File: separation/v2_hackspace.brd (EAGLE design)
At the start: 40.6 x 25.4 mm, 14 parts

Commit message: easy traces
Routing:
- net VSENSE: track 0.00 -> 36.5 mm
- net SERVO: track 0.00 -> 15.4 mm
- net VBAT: track 0.00 -> 13.2 mm
- net BUZZ: track 0.00 -> 9.01 mm
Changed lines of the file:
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@@
 <contactref element="SERCON" pad="2"/>
 <contactref element="C2" pad="2"/>
+<wire x1="-14.986" y1="3.556" x2="-14.986" y2="8.509" width="2.032" layer="16"/>
+<wire x1="-14.986" y1="8.509" x2="-15.113" y2="8.636" width="2.032" layer="16"/>
+<wire x1="-14.986" y1="3.556" x2="-14.986" y2="2.286" width="1.016" layer="16"/>
+<wire x1="-13.716" y1="1.016" x2="-11.684" y2="1.016" width="1.016" layer="16"/>
+<wire x1="-11.684" y1="1.016" x2="-9.661025" y2="3.038975" width="1.016" layer="16"/>
+<wire x1="-9.661025" y1="3.038975" x2="-9.661025" y2="3.184025" width="1.016" layer="16"/>
+<wire x1="-14.986" y1="2.286" x2="-13.716" y2="1.016" width="1.016" layer="16"/>
 <wire x1="-9.661025" y1="3.184025" x2="14.224" y2="14.605" width="0" layer="19" extent="1-1"/>
-<wire x1="-14.986" y1="3.556" x2="-9.661025" y2="3.184025" width="0" layer="19" extent="1-1"/>
-<wire x1="-15.113" y1="8.636" x2="-14.986" y2="3.556" width="0" layer="19" extent="1-1"/>
 <wire x1="-14.859" y1="19.431" x2="-15.113" y2="8.636" width="0" layer="19" extent="1-1"/>
 </signal>
@@
 <contactref element="SERCON" pad="3"/>
 <contactref element="MCU-L" pad="3"/>
-<wire x1="-7.62" y1="15.4305" x2="-12.446" y2="3.556" width="0" layer="19" extent="1-1"/>
+<wire x1="-12.446" y1="3.556" x2="-12.446" y2="13.208" width="1.016" layer="16"/>
+<wire x1="-12.446" y1="13.208" x2="-10.2235" y2="15.4305" width="1.016" layer="16"/>
+<wire x1="-10.2235" y1="15.4305" x2="-7.62" y2="15.4305" width="1.016" layer="16"/>
 </signal>
 <signal name="BUZZ">
 <contactref element="LOUD" pad="1"/>
 <contactref element="MCU-R" pad="3"/>
-<wire x1="13.335" y1="6.35" x2="7.62" y2="10.3505" width="0" layer="19" extent="1-1"/>
+<wire x1="13.335" y1="6.35" x2="13.335" y2="9.144" width="1.016" layer="16"/>
+<wire x1="13.335" y1="9.144" x2="12.1285" y2="10.3505" width="1.016" layer="16"/>
+<wire x1="12.1285" y1="10.3505" x2="7.62" y2="10.3505" width="1.016" layer="16"/>
 </signal>
 <signal name="VSENSE">
@@
 <contactref element="R2" pad="1"/>
 <contactref element="MCU-L" pad="2"/>
-<wire x1="-7.864971875" y1="1.387971875" x2="-7.62" y2="17.9705" width="0" layer="19" extent="1-1"/>
-<wire x1="8.118971875" y1="1.387971875" x2="-7.864971875" y2="1.387971875" width="0" layer="19" extent="1-1"/>
+<wire x1="-7.864971875" y1="1.387971875" x2="-6.232028125" y2="1.387971875" width="1.016" layer="16"/>
+<wire x1="-6.232028125" y1="1.387971875" x2="-3.81" y2="3.81" width="1.016" layer="16"/>
+<wire x1="-3.81" y1="3.81" x2="-3.81" y2="16.51" width="1.016" layer="16"/>
+<wire x1="-3.81" y1="16.51" x2="-5.2705" y2="17.9705" width="1.016" layer="16"/>
+<wire x1="-5.2705" y1="17.9705" x2="-7.62" y2="17.9705" width="1.016" layer="16"/>
+<wire x1="-6.232028125" y1="1.387971875" x2="8.118971875" y2="1.387971875" width="1.016" layer="16"/>
 </signal>
 <signal name="A0">

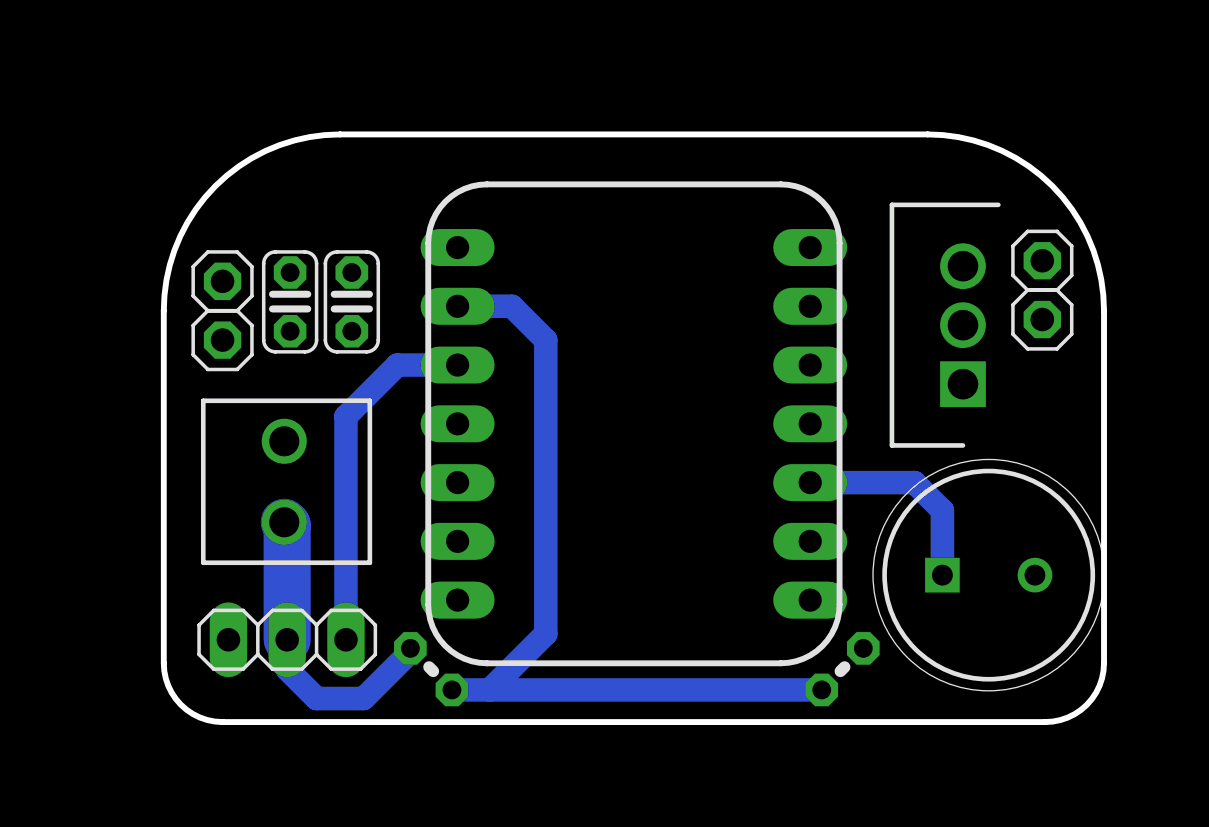
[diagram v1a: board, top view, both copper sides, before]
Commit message: remove spare breakouts
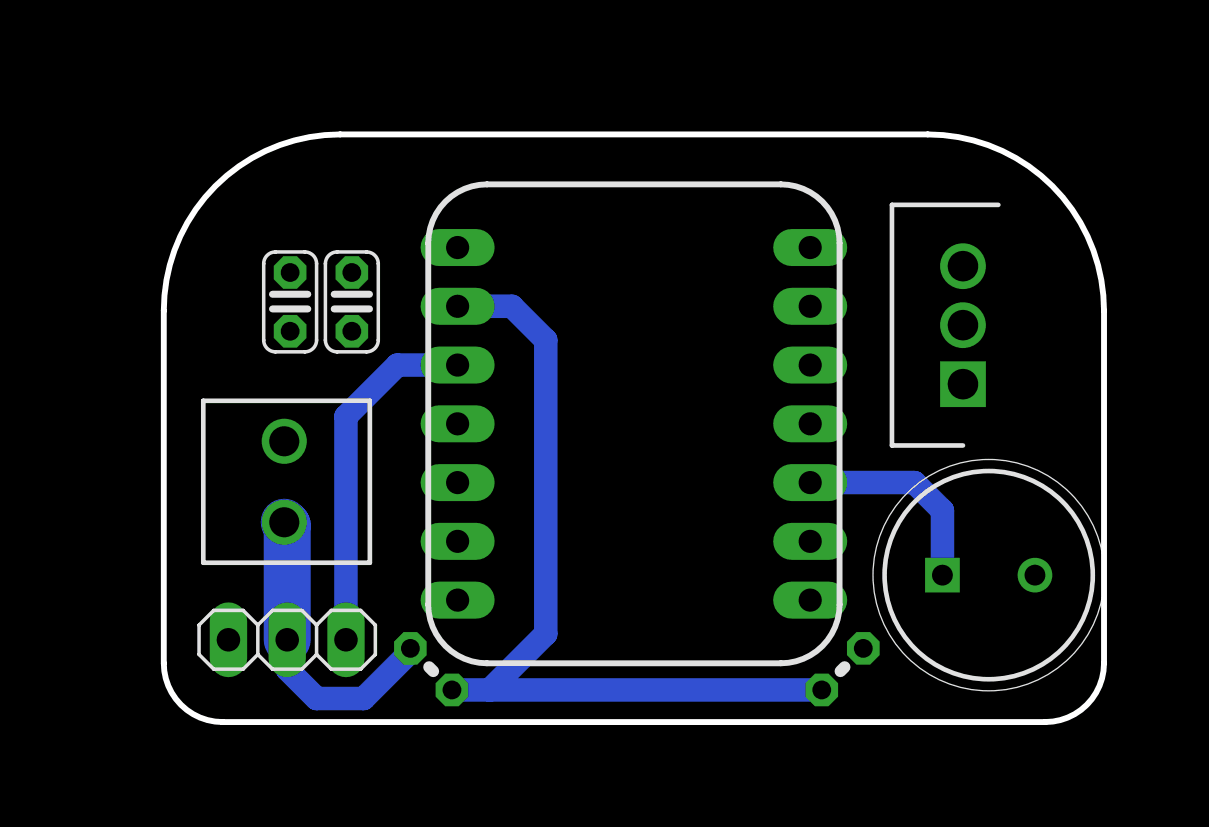
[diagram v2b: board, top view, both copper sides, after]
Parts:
- removed JP1, JP2, JP3, JP4: (no value), pinhead:1X01
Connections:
- net GND: no longer JP1.1
- net SCL: no longer JP3.1
- net SDA: no longer JP2.1
- net VCC: no longer JP4.1
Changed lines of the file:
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@@
 <attribute name="SPICEPREFIX" value="R" x="9.017" y="2.286" size="1.778" layer="27" font="vector" ratio="15" rot="R45" display="off"/>
-</element>
-<element name="JP2" library="pinhead" library_urn="urn:adsk.eagle:library:325" package="1X01" package3d_urn="urn:adsk.eagle:package:22485/2" value="" x="-17.78" y="19.05" smashed="yes">
-<attribute name="POPULARITY" value="64" x="-17.78" y="19.05" size="0.8382" layer="27" font="vector" display="off"/>
-<attribute name="VALUE" x="-19.05" y="15.875" size="1.27" layer="27"/>
-</element>
-<element name="JP3" library="pinhead" library_urn="urn:adsk.eagle:library:325" package="1X01" package3d_urn="urn:adsk.eagle:package:22485/2" value="" x="-17.78" y="16.51" smashed="yes">
-<attribute name="POPULARITY" value="64" x="-17.78" y="16.51" size="0.8382" layer="27" font="vector" display="off"/>
-<attribute name="VALUE" x="-19.05" y="13.335" size="1.27" layer="27"/>
-</element>
-<element name="JP1" library="pinhead" library_urn="urn:adsk.eagle:library:325" package="1X01" package3d_urn="urn:adsk.eagle:package:22485/2" value="" x="17.653" y="17.399" smashed="yes">
-<attribute name="POPULARITY" value="64" x="17.653" y="17.399" size="0.8382" layer="27" font="vector" display="off"/>
-<attribute name="VALUE" x="16.383" y="14.224" size="1.27" layer="27"/>
-</element>
-<element name="JP4" library="pinhead" library_urn="urn:adsk.eagle:library:325" package="1X01" package3d_urn="urn:adsk.eagle:package:22485/2" value="" x="17.653" y="19.939" smashed="yes">
-<attribute name="POPULARITY" value="64" x="17.653" y="19.939" size="0.8382" layer="27" font="vector" display="off"/>
-<attribute name="VALUE" x="16.383" y="16.764" size="1.27" layer="27"/>
 </element>
 <element name="C1" library="rcl" library_urn="urn:adsk.eagle:library:334" package="C025-024X044" package3d_urn="urn:adsk.eagle:package:23630/1" value="100nF" x="-12.192" y="18.161" smashed="yes" rot="R90">
@@
 <contactref element="SERCON" pad="1"/>
 <contactref element="LDO" pad="2"/>
-<contactref element="JP1" pad="1"/>
 <contactref element="C1" pad="1"/>
 <contactref element="C2" pad="1"/>
-<wire x1="14.224" y1="17.155" x2="17.653" y2="17.399" width="0" layer="19" extent="1-1"/>
 <wire x1="7.62" y1="17.9705" x2="14.224" y2="17.155" width="0" layer="19" extent="1-1"/>
-<wire x1="17.335" y1="6.35" x2="17.653" y2="17.399" width="0" layer="19" extent="1-1"/>
+<wire x1="17.335" y1="6.35" x2="14.224" y2="17.155" width="0" layer="19" extent="1-1"/>
 <wire x1="9.915025" y1="3.184025" x2="17.335" y2="6.35" width="0" layer="19" extent="1-1"/>
 <wire x1="-12.192" y1="16.891" x2="7.62" y2="17.9705" width="0" layer="19" extent="1-1"/>
@@
 <signal name="SDA">
 <contactref element="MCU-L" pad="5"/>
-<contactref element="JP2" pad="1"/>
-<wire x1="-17.78" y1="19.05" x2="-7.62" y2="10.3505" width="0" layer="19" extent="1-1"/>
 </signal>
 <signal name="SCL">
 <contactref element="MCU-L" pad="6"/>
-<contactref element="JP3" pad="1"/>
-<wire x1="-7.62" y1="7.8105" x2="-17.78" y2="16.51" width="0" layer="19" extent="1-1"/>
 </signal>
 <signal name="VCC" class="1">
 <contactref element="MCU-R" pad="7"/>
 <contactref element="LDO" pad="3"/>
-<contactref element="JP4" pad="1"/>
 <contactref element="C1" pad="2"/>
-<wire x1="14.224" y1="19.705" x2="17.653" y2="19.939" width="0" layer="19" extent="1-1"/>
 <wire x1="7.62" y1="20.5105" x2="14.224" y2="19.705" width="0" layer="19" extent="1-1"/>
 <wire x1="-12.192" y1="19.431" x2="7.62" y2="20.5105" width="0" layer="19" extent="1-1"/>

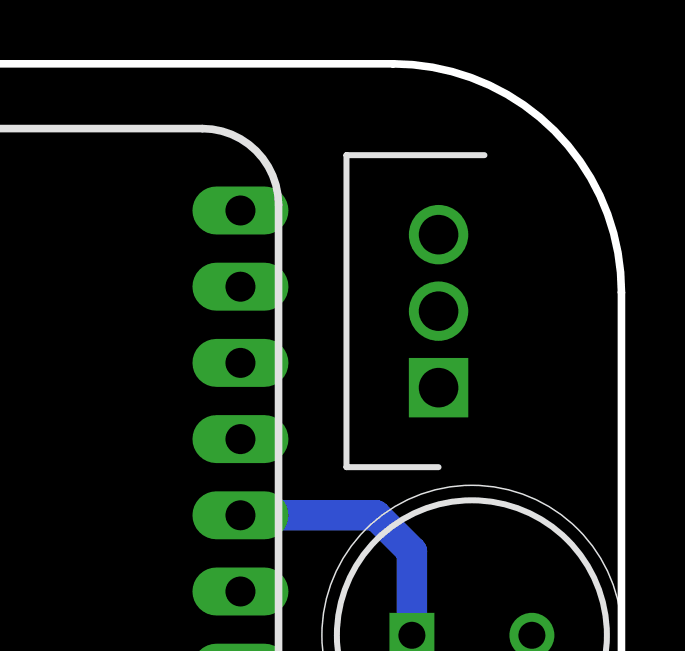
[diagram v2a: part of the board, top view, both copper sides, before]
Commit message: rotate regulator
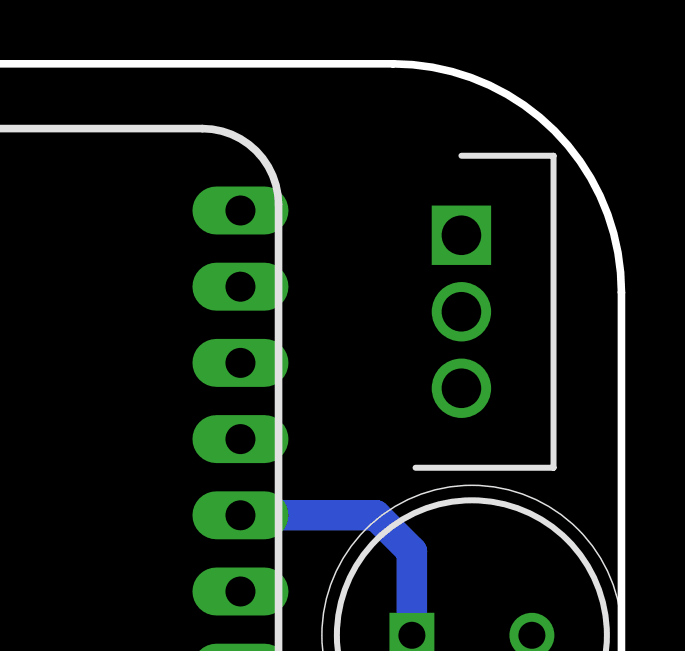
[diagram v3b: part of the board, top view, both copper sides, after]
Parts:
- moved LDO 5.14 mm to (15.0, 19.7), turned to 270 degrees
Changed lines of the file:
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@@
 <attribute name="RS_PRICE-STOCK" value="" x="13.335" y="6.35" size="1.778" layer="27" font="vector" ratio="15" display="off"/>
 </element>
-<element name="LDO" library="SamacSys_Parts" package="TO255P460X1020X2008-3P" package3d_urn="urn:adsk.eagle:package:34276127/2" value="L7805ACV" x="14.224" y="14.605" smashed="yes" rot="R90">
-<attribute name="ALLIED_NUMBER" value="70013701" x="14.224" y="14.605" size="1.778" layer="27" font="vector" ratio="15" rot="R90" display="off"/>
-<attribute name="DESCRIPTION" value="Linear voltage regulator,L7805ACV 5V 1A STMicroelectronics L7805ACV, Single Linear Voltage Regulator, 1A 5 V, 2%, 3-Pin TO-220" x="14.224" y="14.605" size="1.778" layer="27" font="vector" ratio="15" rot="R90" display="off"/>
-<attribute name="HEIGHT" value="4.6mm" x="14.224" y="14.605" size="1.778" layer="27" font="vector" ratio="15" rot="R90" display="off"/>
-<attribute name="MANUFACTURER_NAME" value="STMicroelectronics" x="14.224" y="14.605" size="1.778" layer="27" font="vector" ratio="15" rot="R90" display="off"/>
-<attribute name="MANUFACTURER_PART_NUMBER" value="L7805ACV" x="14.224" y="14.605" size="1.778" layer="27" font="vector" ratio="15" rot="R90" display="off"/>
-<attribute name="RS_PART_NUMBER" value="2988508P" x="14.224" y="14.605" size="1.778" layer="27" font="vector" ratio="15" rot="R90" display="off"/>
-<attribute name="RS_PRICE-STOCK" value="http://uk.rs-online.com/web/p/products/2988508P" x="14.224" y="14.605" size="1.778" layer="27" font="vector" ratio="15" rot="R90" display="off"/>
+<element name="LDO" library="SamacSys_Parts" package="TO255P460X1020X2008-3P" package3d_urn="urn:adsk.eagle:package:34276127/2" value="L7805ACV" x="14.986" y="19.685" smashed="yes" rot="R270">
+<attribute name="ALLIED_NUMBER" value="70013701" x="14.986" y="19.685" size="1.778" layer="27" font="vector" ratio="15" rot="R270" display="off"/>
+<attribute name="DESCRIPTION" value="Linear voltage regulator,L7805ACV 5V 1A STMicroelectronics L7805ACV, Single Linear Voltage Regulator, 1A 5 V, 2%, 3-Pin TO-220" x="14.986" y="19.685" size="1.778" layer="27" font="vector" ratio="15" rot="R270" display="off"/>
+<attribute name="HEIGHT" value="4.6mm" x="14.986" y="19.685" size="1.778" layer="27" font="vector" ratio="15" rot="R270" display="off"/>
+<attribute name="MANUFACTURER_NAME" value="STMicroelectronics" x="14.986" y="19.685" size="1.778" layer="27" font="vector" ratio="15" rot="R270" display="off"/>
+<attribute name="MANUFACTURER_PART_NUMBER" value="L7805ACV" x="14.986" y="19.685" size="1.778" layer="27" font="vector" ratio="15" rot="R270" display="off"/>
+<attribute name="RS_PART_NUMBER" value="2988508P" x="14.986" y="19.685" size="1.778" layer="27" font="vector" ratio="15" rot="R270" display="off"/>
+<attribute name="RS_PRICE-STOCK" value="http://uk.rs-online.com/web/p/products/2988508P" x="14.986" y="19.685" size="1.778" layer="27" font="vector" ratio="15" rot="R270" display="off"/>
 </element>
 <element name="BAT" library="SamacSys_Parts" package="MB332350M02SZ" value="MB332-350M02SZ" x="-15.113" y="8.636" smashed="yes" rot="R90">
@@
 <contactref element="C1" pad="1"/>
 <contactref element="C2" pad="1"/>
-<wire x1="7.62" y1="17.9705" x2="14.224" y2="17.155" width="0" layer="19" extent="1-1"/>
-<wire x1="17.335" y1="6.35" x2="14.224" y2="17.155" width="0" layer="19" extent="1-1"/>
+<wire x1="7.62" y1="17.9705" x2="14.986" y2="17.135" width="0" layer="19" extent="1-1"/>
+<wire x1="17.335" y1="6.35" x2="14.986" y2="17.135" width="0" layer="19" extent="1-1"/>
 <wire x1="9.915025" y1="3.184025" x2="17.335" y2="6.35" width="0" layer="19" extent="1-1"/>
 <wire x1="-12.192" y1="16.891" x2="7.62" y2="17.9705" width="0" layer="19" extent="1-1"/>
@@
 <contactref element="LDO" pad="3"/>
 <contactref element="C1" pad="2"/>
-<wire x1="7.62" y1="20.5105" x2="14.224" y2="19.705" width="0" layer="19" extent="1-1"/>
+<wire x1="7.62" y1="20.5105" x2="14.986" y2="14.585" width="0" layer="19" extent="1-1"/>
 <wire x1="-12.192" y1="19.431" x2="7.62" y2="20.5105" width="0" layer="19" extent="1-1"/>
 </signal>
@@
 <wire x1="-9.661025" y1="3.038975" x2="-9.661025" y2="3.184025" width="1.016" layer="16"/>
 <wire x1="-14.986" y1="2.286" x2="-13.716" y2="1.016" width="1.016" layer="16"/>
-<wire x1="-9.661025" y1="3.184025" x2="14.224" y2="14.605" width="0" layer="19" extent="1-1"/>
+<wire x1="-9.661025" y1="3.184025" x2="14.986" y2="19.685" width="0" layer="19" extent="1-1"/>
 <wire x1="-14.859" y1="19.431" x2="-15.113" y2="8.636" width="0" layer="19" extent="1-1"/>
 </signal>

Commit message: complete reconnecting
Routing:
- net VBAT: track 13.2 -> 62.3 mm
- net VCC: track 0.00 -> 34.3 mm
- added copper zone on layer 16, net GND
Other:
- board text removed: "VSENSE"
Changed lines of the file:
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@@
 <dimension x1="-20.32" y1="-2.54" x2="20.32" y2="-2.54" x3="0" y3="-6.35" textsize="1.778" layer="47" visible="yes"/>
 <dimension x1="22.86" y1="0" x2="22.86" y2="25.4" x3="27.94" y3="12.7" textsize="1.778" layer="47" visible="yes"/>
-<text x="-5.715" y="21.463" size="0.508" layer="22" font="vector" ratio="12" rot="MR0">VSENSE</text>
 </plain>
 <attributes>
@@
 <contactref element="C1" pad="1"/>
 <contactref element="C2" pad="1"/>
-<wire x1="7.62" y1="17.9705" x2="14.986" y2="17.135" width="0" layer="19" extent="1-1"/>
-<wire x1="17.335" y1="6.35" x2="14.986" y2="17.135" width="0" layer="19" extent="1-1"/>
-<wire x1="9.915025" y1="3.184025" x2="17.335" y2="6.35" width="0" layer="19" extent="1-1"/>
-<wire x1="-12.192" y1="16.891" x2="7.62" y2="17.9705" width="0" layer="19" extent="1-1"/>
-<wire x1="-14.859" y1="16.891" x2="-12.192" y2="16.891" width="0" layer="19" extent="1-1"/>
-<wire x1="-15.113" y1="12.136" x2="-14.859" y2="16.891" width="0" layer="19" extent="1-1"/>
+<polygon width="1.016" layer="16" spacing="0.508">
+<vertex x="-25.4" y="29.21"/>
+<vertex x="19.05" y="29.21"/>
+<vertex x="22.86" y="25.4"/>
+<vertex x="22.86" y="0"/>
+<vertex x="20.32" y="-2.54"/>
+<vertex x="-20.32" y="-2.54"/>
+<vertex x="-25.4" y="2.54"/>
+</polygon>
 <wire x1="-17.526" y1="3.556" x2="-15.113" y2="12.136" width="0" layer="19" extent="1-1"/>
+<wire x1="7.62" y1="17.9705" x2="-12.192" y2="16.891" width="0" layer="19" extent="1-1"/>
 </signal>
 <signal name="MOSI">
@@
 <contactref element="LDO" pad="3"/>
 <contactref element="C1" pad="2"/>
-<wire x1="7.62" y1="20.5105" x2="14.986" y2="14.585" width="0" layer="19" extent="1-1"/>
-<wire x1="-12.192" y1="19.431" x2="7.62" y2="20.5105" width="0" layer="19" extent="1-1"/>
+<wire x1="14.986" y1="14.585" x2="12.085" y2="14.585" width="1.016" layer="16"/>
+<wire x1="12.085" y1="14.585" x2="11.43" y2="15.24" width="1.016" layer="16"/>
+<wire x1="11.43" y1="15.24" x2="11.43" y2="19.05" width="1.016" layer="16"/>
+<wire x1="11.43" y1="19.05" x2="9.9695" y2="20.5105" width="1.016" layer="16"/>
+<wire x1="9.9695" y1="20.5105" x2="7.62" y2="20.5105" width="1.016" layer="16"/>
+<wire x1="-12.192" y1="19.431" x2="-12.192" y2="19.558" width="1.016" layer="16"/>
+<wire x1="3.6195" y1="20.5105" x2="7.62" y2="20.5105" width="1.016" layer="16"/>
+<wire x1="-12.192" y1="19.558" x2="-8.89" y2="22.86" width="1.016" layer="16"/>
+<wire x1="-8.89" y1="22.86" x2="1.27" y2="22.86" width="1.016" layer="16"/>
+<wire x1="1.27" y1="22.86" x2="3.6195" y2="20.5105" width="1.016" layer="16"/>
 </signal>
 <signal name="+3V3">
@@
 <wire x1="-9.661025" y1="3.038975" x2="-9.661025" y2="3.184025" width="1.016" layer="16"/>
 <wire x1="-14.986" y1="2.286" x2="-13.716" y2="1.016" width="1.016" layer="16"/>
-<wire x1="-9.661025" y1="3.184025" x2="14.986" y2="19.685" width="0" layer="19" extent="1-1"/>
-<wire x1="-14.859" y1="19.431" x2="-15.113" y2="8.636" width="0" layer="19" extent="1-1"/>
+<wire x1="14.986" y1="19.685" x2="10.541" y2="24.13" width="1.016" layer="16"/>
+<wire x1="-10.16" y1="24.13" x2="-14.859" y2="19.431" width="1.016" layer="16"/>
+<wire x1="10.541" y1="24.13" x2="-10.16" y2="24.13" width="1.016" layer="16"/>
+<wire x1="-14.859" y1="19.431" x2="-17.399" y2="19.431" width="1.016" layer="16"/>
+<wire x1="-17.399" y1="19.431" x2="-17.78" y2="19.05" width="1.016" layer="16"/>
+<wire x1="-17.78" y1="19.05" x2="-17.78" y2="10.16" width="1.016" layer="16"/>
+<wire x1="-17.78" y1="10.16" x2="-16.129" y2="8.509" width="1.016" layer="16"/>
+<wire x1="-16.129" y1="8.509" x2="-14.986" y2="8.509" width="1.016" layer="16"/>
 </signal>
 <signal name="SERVO">
